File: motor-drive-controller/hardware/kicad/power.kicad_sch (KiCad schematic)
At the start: 11 parts, among them U4 LMR51610XDBVR

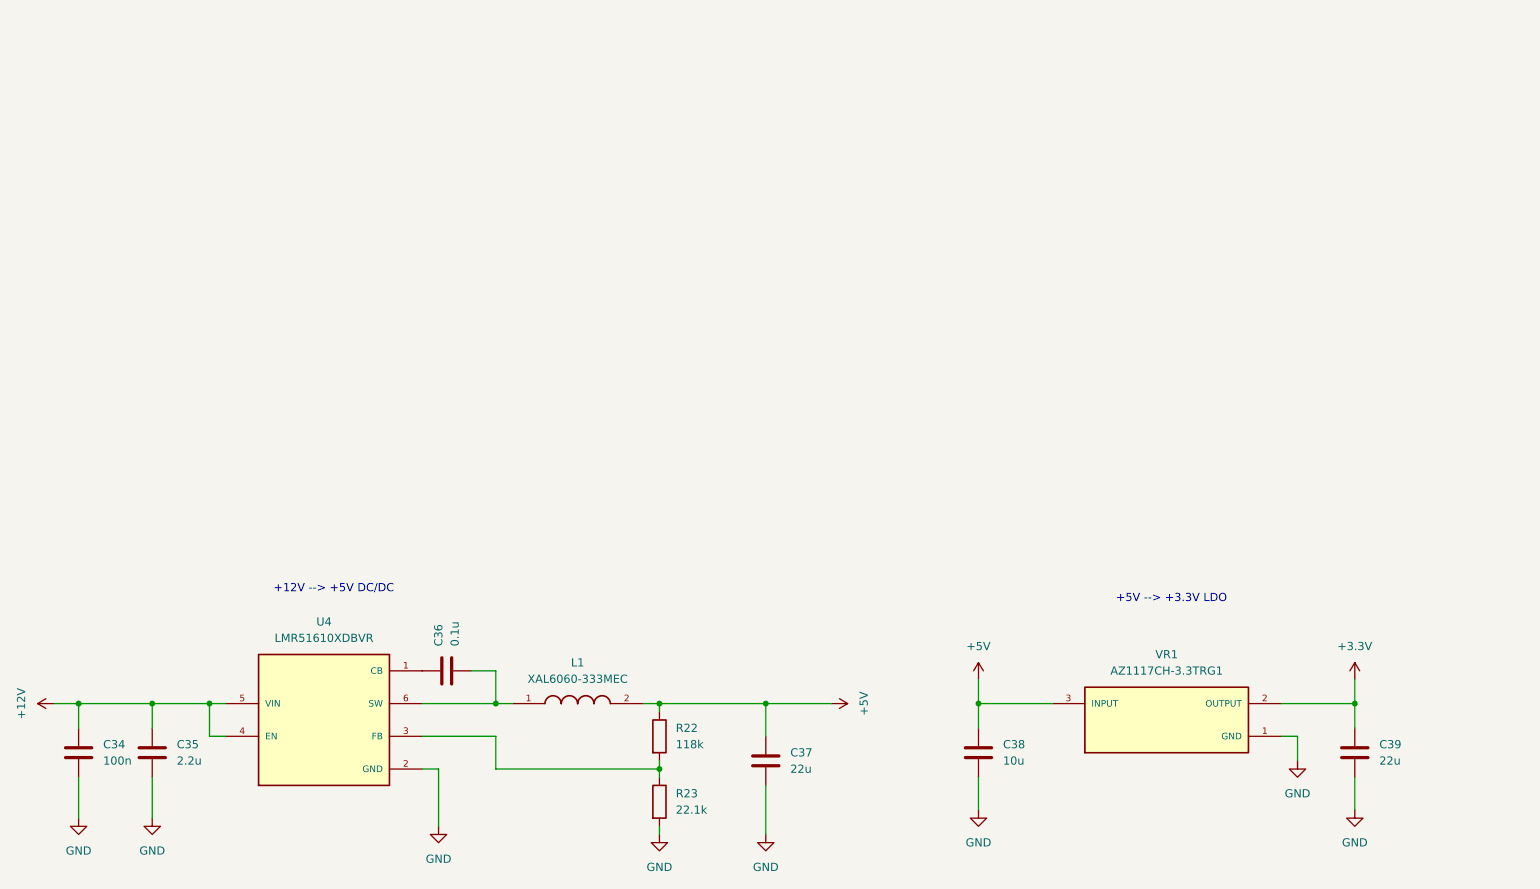
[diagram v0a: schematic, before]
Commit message: feat(hw10): component selection and add Power schema
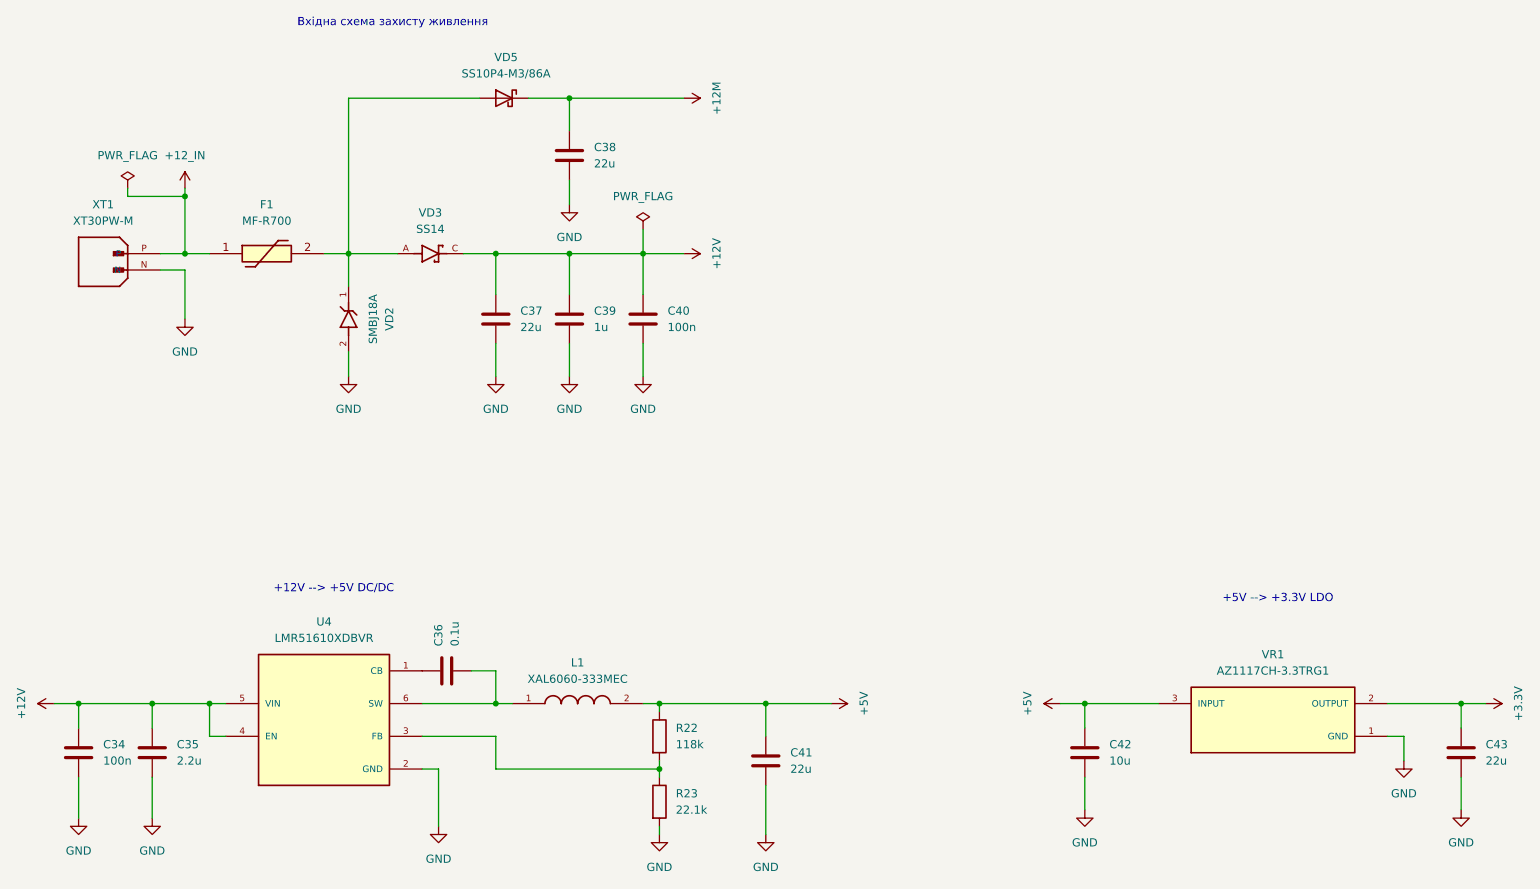
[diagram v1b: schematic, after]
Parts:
- added C37, C38: 22u, Capacitor_SMD:C_1210_3225Metric, symbol Device:C
- added C39: 1u, Capacitor_SMD:C_0603_1608Metric, symbol Device:C
- added C40: 100n, Capacitor_SMD:C_0603_1608Metric, symbol Device:C
- added F1: MF-R700, LIB_MF-R700:MFR700, symbol MF-R700:MF-R700
- added VD2: SMBJ18A, SMBJ18A:DIOM5436X261N, symbol SMBJ18A:SMBJ18A
- added VD3: SS14, SS14:DIOM4325X250N, symbol SS14:SS14
- added VD5: SS10P4-M3/86A, Package_TO_SOT_SMD:TO-277A, symbol Device:D_Schottky
- added XT1: XT30PW-M, XT30PW-M:AMASS_XT30PW-M, symbol XT30PW-M:XT30PW-M
- renumbered C37 to C41, C38 to C42, C39 to C43
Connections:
- net +12V: now also C37.1, C39.1, C40.1, VD3.C
- net GND: now also C37.2, C38.2, C39.2, C40.2, VD2.2, XT1.N
- new net: F1.2, VD2.1, VD3.A, VD5.2 (A)
- new net +12M: C38.1, VD5.1 (K)
- new net +12_IN: F1.1, XT1.P
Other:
- note added: "Вхідна схема захисту живлення"
- title: (none) -> Power
- moved on the sheet: C42, C43, VR1

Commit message: feat(hw10): update capacitor value to 0.1u and add voltage property for components
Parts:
- C34: value 100n -> 0.1u; Voltage (none) -> 25V
- C36: Voltage (none) -> 25V
- C40: value 100n -> 0.1u
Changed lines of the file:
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@@
 			)
 		)
-		(property "Value" "100n"
+		(property "Value" "0.1u"
 			(at 34.29 135.8899 0)
 			(show_name no)
@@
 		)
 		(property "Description" "Unpolarized capacitor"
+			(at 30.48 134.62 0)
+			(hide yes)
+			(show_name no)
+			(do_not_autoplace no)
+			(effects
+				(font
+					(size 1.27 1.27)
+				)
+			)
+		)
+		(property "Voltage" "25V"
 			(at 30.48 134.62 0)
 			(hide yes)
@@
 			)
 		)
-		(property "Value" "100n"
+		(property "Value" "0.1u"
 			(at 121.92 68.5799 0)
 			(show_name no)
@@
 			(at 87.63 121.92 0)
 			(hide yes)
+			(show_name no)
+			(do_not_autoplace no)
+			(effects
+				(font
+					(size 1.27 1.27)
+				)
+			)
+		)
+		(property "Voltage" "25V"
+			(at 87.63 121.92 0)
+			(hide yes)

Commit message: feat(hw10): add SS10P4 Schottky diode footprint and symbol to the project
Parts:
- removed VD5: SS10P4-M3/86A, Package_TO_SOT_SMD:TO-277A, symbol Device:D_Schottky
- added VD5: SS10P4-M3/86A, SS10P4:SMPC_TO-277A, symbol SS10P4:SS10P4
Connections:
- net +12M: now also VD5.C
- net at F1.2, VD2.1, VD3.A: now also VD5.A
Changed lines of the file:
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@@
 	)
 	(junction
-		(at 106.68 33.02)
-		(diameter 0)
-		(color 0 0 0 0)
-	)
-	(junction
 		(at 120.65 137.16)
 		(diameter 0)
@@
 	)
 	(junction
+		(at 106.68 33.02)
+		(diameter 0)
+		(color 0 0 0 0)
+	)
+	(junction
 		(at 95.25 57.15)
 		(diameter 0)
@@
 	(wire
 		(pts
-			(xy 100.33 33.02) (xy 106.68 33.02)
+			(xy 118.11 57.15) (xy 124.46 57.15)
 		)
 		(stroke
@@
 	(wire
 		(pts
-			(xy 118.11 57.15) (xy 124.46 57.15)
+			(xy 248.92 127) (xy 245.11 127)
 		)
 		(stroke
@@
 	(wire
 		(pts
-			(xy 248.92 127) (xy 245.11 127)
+			(xy 53.34 132.08) (xy 50.8 132.08)
 		)
 		(stroke
@@
 	(wire
 		(pts
-			(xy 53.34 132.08) (xy 50.8 132.08)
+			(xy 120.65 127) (xy 120.65 128.27)
 		)
 		(stroke
@@
 	(wire
 		(pts
-			(xy 120.65 127) (xy 120.65 128.27)
+			(xy 72.39 57.15) (xy 68.58 57.15)
 		)
 		(stroke
@@
 	(wire
 		(pts
-			(xy 72.39 57.15) (xy 68.58 57.15)
+			(xy 30.48 138.43) (xy 30.48 144.78)
 		)
 		(stroke
@@
 	(wire
 		(pts
-			(xy 30.48 138.43) (xy 30.48 144.78)
+			(xy 72.39 33.02) (xy 90.17 33.02)
 		)
 		(stroke
@@
 	(wire
 		(pts
-			(xy 92.71 33.02) (xy 72.39 33.02)
-		)
-		(stroke
-			(width 0)
-			(type default)
-		)
-	)
-	(wire
-		(pts
 			(xy 72.39 62.23) (xy 72.39 57.15)
 		)
@@
 	(wire
 		(pts
+			(xy 100.33 33.02) (xy 106.68 33.02)
+		)
+		(stroke
+			(width 0)
+			(type default)
+		)
+	)
+	(wire
+		(pts
 			(xy 46.99 59.69) (xy 43.18 59.69)
 		)
@@
 	)
 	(symbol
+		(lib_id "SS10P4:SS10P4")
+		(at 95.25 33.02 0)
+		(unit 1)
+		(body_style 1)
+		(exclude_from_sim no)
+		(in_bom yes)
+		(on_board yes)
+		(in_pos_files yes)
+		(dnp no)
+		(fields_autoplaced yes)
+		(property "Reference" "VD5"
+			(at 95.25 26.67 0)
+			(show_name no)
+			(do_not_autoplace no)
+			(effects
+				(font
+					(size 1.27 1.27)
+				)
+			)
+		)
+		(property "Value" "SS10P4-M3/86A"
+			(at 95.25 29.21 0)
+			(show_name no)
+			(do_not_autoplace no)
+			(effects
+				(font
+					(size 1.27 1.27)
+				)
+			)
+		)
+		(property "Footprint" "SS10P4:SMPC_TO-277A"
+			(at 95.25 33.02 0)
+			(hide yes)
+			(show_name no)
+			(do_not_autoplace no)
+			(effects
+				(font
+					(size 1.27 1.27)
+				)
+				(justify bottom)
+			)
+		)
+		(property "Datasheet" "https://www.vishay.com/docs/88983/ss10p4.pdf"
+			(at 95.25 33.02 0)
+			(hide yes)
+			(show_name no)
+			(do_not_autoplace no)
+			(effects
+				(font
+					(size 1.27 1.27)
+				)
+				(justify bottom)
+			)
+		)
+		(property "Description" "Schottky 10 A, 40 V, VF 0.41 V @ 5 A, eSMP SMPC (TO-277A)"
+			(at 95.25 33.02 0)
+			(hide yes)
+			(show_name no)
+			(do_not_autoplace no)
+			(effects
+				(font
+					(size 1.27 1.27)
+				)
+				(justify bottom)
+			)
+		)
+		(property "MF" "Vishay General Semiconductor"
+			(at 95.25 33.02 0)
+			(hide yes)
+			(show_name no)
+			(do_not_autoplace no)
+			(effects
+				(font
+					(size 1.27 1.27)
+				)
+				(justify bottom)
+			)
+		)
+		(property "MAXIMUM_PACKAGE_HEIGHT" "1.2 mm"
+			(at 95.25 33.02 0)
+			(hide yes)
+			(show_name no)
+			(do_not_autoplace no)
+			(effects
+				(font
+					(size 1.27 1.27)
+				)
+				(justify bottom)
+			)
+		)
+		(property "Package" "SMPC (TO-277A)"
+			(at 95.25 33.02 0)
+			(hide yes)
+			(show_name no)
+			(do_not_autoplace no)
+			(effects
+				(font
+					(size 1.27 1.27)
+				)
+				(justify bottom)
+			)
+		)
+		(property "MP" "SS10P4-M3/86A"
+			(at 95.25 33.02 0)
+			(hide yes)
+			(show_name no)
+			(do_not_autoplace no)
+			(effects
+				(font
+					(size 1.27 1.27)
+				)
+				(justify bottom)
+			)
+		)
+		(property "MANUFACTURER" "Vishay General Semiconductor"
+			(at 95.25 33.02 0)
+			(hide yes)
+			(show_name no)
+			(do_not_autoplace no)
+			(effects
+				(font
+					(size 1.27 1.27)
+				)
+				(justify bottom)
+			)
+		)
+		(pin "C"
+		)
+		(pin "A"
+		)
+		(instances
+			(project "motor-drive-controller"
+				(path "/b8e0307a-d356-4cd3-91c6-dd251b6e910b/4f45cab3-b4c2-456a-894e-61f49c3959a4"
+					(reference "VD5")
+					(unit 1)
+				)
+			)
+		)
+	)
+	(symbol
 		(lib_id "power:+12V")
 		(at 46.99 46.99 0)
@@
 					(unit 1)
 				)
-			)
-		)
-	)
-	(symbol
-		(lib_id "Device:D_Schottky")
-		(at 96.52 33.02 0)
-		(mirror y)
-		(unit 1)
-		(body_style 1)
-		(exclude_from_sim no)
-		(in_bom yes)
-		(on_board yes)
-		(in_pos_files yes)
-		(dnp no)
-		(fields_autoplaced yes)
-		(property "Reference" "VD5"
-			(at 96.8375 26.67 0)
-			(show_name no)
-			(do_not_autoplace no)
-			(effects
-				(font
-					(size 1.27 1.27)
-				)
-			)
-		)
-		(property "Value" "SS10P4-M3/86A"
-			(at 96.8375 29.21 0)
-			(show_name no)
-			(do_not_autoplace no)
-			(effects
-				(font
-					(size 1.27 1.27)
-				)
-			)
-		)
-		(property "Footprint" "Package_TO_SOT_SMD:TO-277A"
-			(at 96.52 33.02 0)
-			(hide yes)
-			(show_name no)
-			(do_not_autoplace no)
-			(effects
-				(font
-					(size 1.27 1.27)
-				)
-			)
-		)
-		(property "Datasheet" "https://www.vishay.com/docs/88983/ss10p4.pdf"
-			(at 96.52 33.02 0)
-			(hide yes)
-			(show_name no)
-			(do_not_autoplace no)
-			(effects
-				(font
-					(size 1.27 1.27)
-				)
-			)
-		)
-		(property "Description" "Schottky diode"
-			(at 96.52 33.02 0)
-			(hide yes)
-			(show_name no)
-			(do_not_autoplace no)
-			(effects
-				(font
-					(size 1.27 1.27)
-				)
-			)
-		)
-		(pin "1"
-		)
-		(pin "2"
-		)
-		(instances
-			(project "motor-drive-controller"
-				(path "/b8e0307a-d356-4cd3-91c6-dd251b6e910b/4f45cab3-b4c2-456a-894e-61f49c3959a4"
-					(reference "VD5")
-					(unit 1)
-				)

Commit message: feat(hw10): replace component from SS10P4 library
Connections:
- net +12M: now also VD5.K (Cathode); no longer VD5.C
- net at F1.2, VD2.1, VD3.A: now also VD5.1 (Anode_1), VD5.2 (Anode_2); no longer VD5.A
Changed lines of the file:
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@@
 	)
 	(junction
+		(at 106.68 33.02)
+		(diameter 0)
+		(color 0 0 0 0)
+	)
+	(junction
 		(at 46.99 57.15)
 		(diameter 0)
@@
 	)
 	(junction
+		(at 78.74 33.02)
+		(diameter 0)
+		(color 0 0 0 0)
+	)
+	(junction
 		(at 120.65 137.16)
 		(diameter 0)
@@
 	)
 	(junction
-		(at 106.68 33.02)
-		(diameter 0)
-		(color 0 0 0 0)
-	)
-	(junction
 		(at 95.25 57.15)
 		(diameter 0)
@@
 	(wire
 		(pts
-			(xy 30.48 138.43) (xy 30.48 144.78)
+			(xy 82.55 35.56) (xy 78.74 35.56)
 		)
 		(stroke
@@
 	(wire
 		(pts
-			(xy 72.39 33.02) (xy 90.17 33.02)
+			(xy 72.39 33.02) (xy 78.74 33.02)
+		)
+		(stroke
+			(width 0)
+			(type default)
+		)
+	)
+	(wire
+		(pts
+			(xy 30.48 138.43) (xy 30.48 144.78)
 		)
 		(stroke
@@
 	(wire
 		(pts
-			(xy 100.33 33.02) (xy 106.68 33.02)
-		)
-		(stroke
-			(width 0)
-			(type default)
-		)
-	)
-	(wire
-		(pts
 			(xy 46.99 59.69) (xy 43.18 59.69)
 		)
@@
 	(wire
 		(pts
+			(xy 97.79 33.02) (xy 106.68 33.02)
+		)
+		(stroke
+			(width 0)
+			(type default)
+		)
+	)
+	(wire
+		(pts
 			(xy 46.99 48.26) (xy 46.99 57.15)
 		)
@@
 	(wire
 		(pts
+			(xy 78.74 35.56) (xy 78.74 33.02)
+		)
+		(stroke
+			(width 0)
+			(type default)
+		)
+	)
+	(wire
+		(pts
+			(xy 78.74 30.48) (xy 78.74 33.02)
+		)
+		(stroke
+			(width 0)
+			(type default)
+		)
+	)
+	(wire
+		(pts
 			(xy 83.82 127) (xy 95.25 127)
 		)
@@
 	(wire
 		(pts
+			(xy 82.55 30.48) (xy 78.74 30.48)
+		)
+		(stroke
+			(width 0)
+			(type default)
+		)
+	)
+	(wire
+		(pts
 			(xy 120.65 135.89) (xy 120.65 137.16)
 		)
@@
 	)
 	(symbol
+		(lib_id "SS10P4:SS10P4")
+		(at 90.17 33.02 0)
+		(mirror y)
+		(unit 1)
+		(body_style 1)
+		(exclude_from_sim no)
+		(in_bom yes)
+		(on_board yes)
+		(in_pos_files yes)
+		(dnp no)
+		(fields_autoplaced yes)
+		(property "Reference" "VD5"
+			(at 90.17 25.4 0)
+			(show_name no)
+			(do_not_autoplace no)
+			(effects
+				(font
+					(size 1.27 1.27)
+				)
+			)
+		)
+		(property "Value" "SS10P4-M3/86A"
+			(at 90.17 27.94 0)
+			(show_name no)
+			(do_not_autoplace no)
+			(effects
+				(font
+					(size 1.27 1.27)
+				)
+			)
+		)
+		(property "Footprint" "SS10P4:SMPC_TO-277A"
+			(at 90.17 33.02 0)
+			(hide yes)
+			(show_name no)
+			(do_not_autoplace no)
+			(effects
+				(font
+					(size 1.27 1.27)
+				)
+				(justify bottom)
+			)
+		)
+		(property "Datasheet" "https://www.vishay.com/docs/88983/ss10p4.pdf"
+			(at 90.17 33.02 0)
+			(hide yes)
+			(show_name no)
+			(do_not_autoplace no)
+			(effects
+				(font
+					(size 1.27 1.27)
+				)
+				(justify bottom)
+			)
+		)
+		(property "Description" "Schottky 10 A, 40 V, VF 0.41 V @ 5 A, eSMP SMPC (TO-277A)"
+			(at 90.17 33.02 0)
+			(hide yes)
+			(show_name no)
+			(do_not_autoplace no)
+			(effects
+				(font
+					(size 1.27 1.27)
+				)
+				(justify bottom)
+			)
+		)
+		(property "MF" "Vishay General Semiconductor"
+			(at 90.17 33.02 0)
+			(hide yes)
+			(show_name no)
+			(do_not_autoplace no)
+			(effects
+				(font
+					(size 1.27 1.27)
+				)
+				(justify bottom)
+			)
+		)
+		(property "MAXIMUM_PACKAGE_HEIGHT" "1.2 mm"
+			(at 90.17 33.02 0)
+			(hide yes)
+			(show_name no)
+			(do_not_autoplace no)
+			(effects
+				(font
+					(size 1.27 1.27)
+				)
+				(justify bottom)
+			)
+		)
+		(property "Package" "SMPC (TO-277A)"
+			(at 90.17 33.02 0)
+			(hide yes)
+			(show_name no)
+			(do_not_autoplace no)
+			(effects
+				(font
+					(size 1.27 1.27)
+				)
+				(justify bottom)
+			)
+		)
+		(property "MP" "SS10P4-M3/86A"
+			(at 90.17 33.02 0)
+			(hide yes)
+			(show_name no)
+			(do_not_autoplace no)
+			(effects
+				(font
+					(size 1.27 1.27)
+				)
+				(justify bottom)
+			)
+		)
+		(property "MANUFACTURER" "Vishay General Semiconductor"
+			(at 90.17 33.02 0)
+			(hide yes)
+			(show_name no)
+			(do_not_autoplace no)
+			(effects
+				(font
+					(size 1.27 1.27)
+				)
+				(justify bottom)
+			)
+		)
+		(pin "2"
+		)
+		(pin "K"
+		)
+		(pin "1"
+		)
+		(instances
+			(project "motor-drive-controller"
+				(path "/b8e0307a-d356-4cd3-91c6-dd251b6e910b/4f45cab3-b4c2-456a-894e-61f49c3959a4"
+					(reference "VD5")
+					(unit 1)
+				)
+			)
+		)
+	)
+	(symbol
 		(lib_id "power:GND")
 		(at 106.68 76.2 0)
@@
 					(unit 1)
 				)
-			)
-		)
-	)
-	(symbol
-		(lib_id "SS10P4:SS10P4")
-		(at 95.25 33.02 0)
-		(unit 1)
-		(body_style 1)
-		(exclude_from_sim no)
-		(in_bom yes)
-		(on_board yes)
-		(in_pos_files yes)
-		(dnp no)
-		(fields_autoplaced yes)
-		(property "Reference" "VD5"
-			(at 95.25 26.67 0)
-			(show_name no)
-			(do_not_autoplace no)
-			(effects
-				(font
-					(size 1.27 1.27)
-				)
-			)
-		)
-		(property "Value" "SS10P4-M3/86A"
-			(at 95.25 29.21 0)
-			(show_name no)
-			(do_not_autoplace no)
-			(effects
-				(font
-					(size 1.27 1.27)
-				)
-			)
-		)
-		(property "Footprint" "SS10P4:SMPC_TO-277A"
-			(at 95.25 33.02 0)
-			(hide yes)
-			(show_name no)
-			(do_not_autoplace no)
-			(effects
-				(font
-					(size 1.27 1.27)
-				)
-				(justify bottom)
-			)
-		)
-		(property "Datasheet" "https://www.vishay.com/docs/88983/ss10p4.pdf"
-			(at 95.25 33.02 0)
-			(hide yes)
-			(show_name no)
-			(do_not_autoplace no)
-			(effects
-				(font
-					(size 1.27 1.27)
-				)
-				(justify bottom)
-			)
-		)
-		(property "Description" "Schottky 10 A, 40 V, VF 0.41 V @ 5 A, eSMP SMPC (TO-277A)"
-			(at 95.25 33.02 0)
-			(hide yes)
-			(show_name no)
-			(do_not_autoplace no)
-			(effects
-				(font
-					(size 1.27 1.27)
-				)
-				(justify bottom)
-			)
-		)
-		(property "MF" "Vishay General Semiconductor"
-			(at 95.25 33.02 0)
-			(hide yes)
-			(show_name no)
-			(do_not_autoplace no)
-			(effects
-				(font
-					(size 1.27 1.27)
-				)
-				(justify bottom)
-			)
-		)
-		(property "MAXIMUM_PACKAGE_HEIGHT" "1.2 mm"
-			(at 95.25 33.02 0)
-			(hide yes)
-			(show_name no)
-			(do_not_autoplace no)
-			(effects
-				(font
-					(size 1.27 1.27)
-				)
-				(justify bottom)
-			)
-		)
-		(property "Package" "SMPC (TO-277A)"
-			(at 95.25 33.02 0)
-			(hide yes)
-			(show_name no)
-			(do_not_autoplace no)
-			(effects
-				(font
-					(size 1.27 1.27)
-				)
-				(justify bottom)
-			)
-		)
-		(property "MP" "SS10P4-M3/86A"
-			(at 95.25 33.02 0)
-			(hide yes)
-			(show_name no)
-			(do_not_autoplace no)
-			(effects
-				(font
-					(size 1.27 1.27)
-				)
-				(justify bottom)
-			)
-		)
-		(property "MANUFACTURER" "Vishay General Semiconductor"
-			(at 95.25 33.02 0)
-			(hide yes)
-			(show_name no)
-			(do_not_autoplace no)
-			(effects
-				(font
-					(size 1.27 1.27)
-				)
-				(justify bottom)
-			)
-		)
-		(pin "C"
-		)
-		(pin "A"
-		)
-		(instances
-			(project "motor-drive-controller"
-				(path "/b8e0307a-d356-4cd3-91c6-dd251b6e910b/4f45cab3-b4c2-456a-894e-61f49c3959a4"
-					(reference "VD5")
-					(unit 1)
-				)
